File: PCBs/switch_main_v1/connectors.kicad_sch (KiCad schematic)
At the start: 14 parts, among them J1101 76825-0004, J1102 PJ-002AH, J1103 Conn_ST_STDC14, Q1101 DMTH6016LPSQ-13, U1101 TVS2701DRBR, U1102 MPQ5850GJ-AEC1-Z

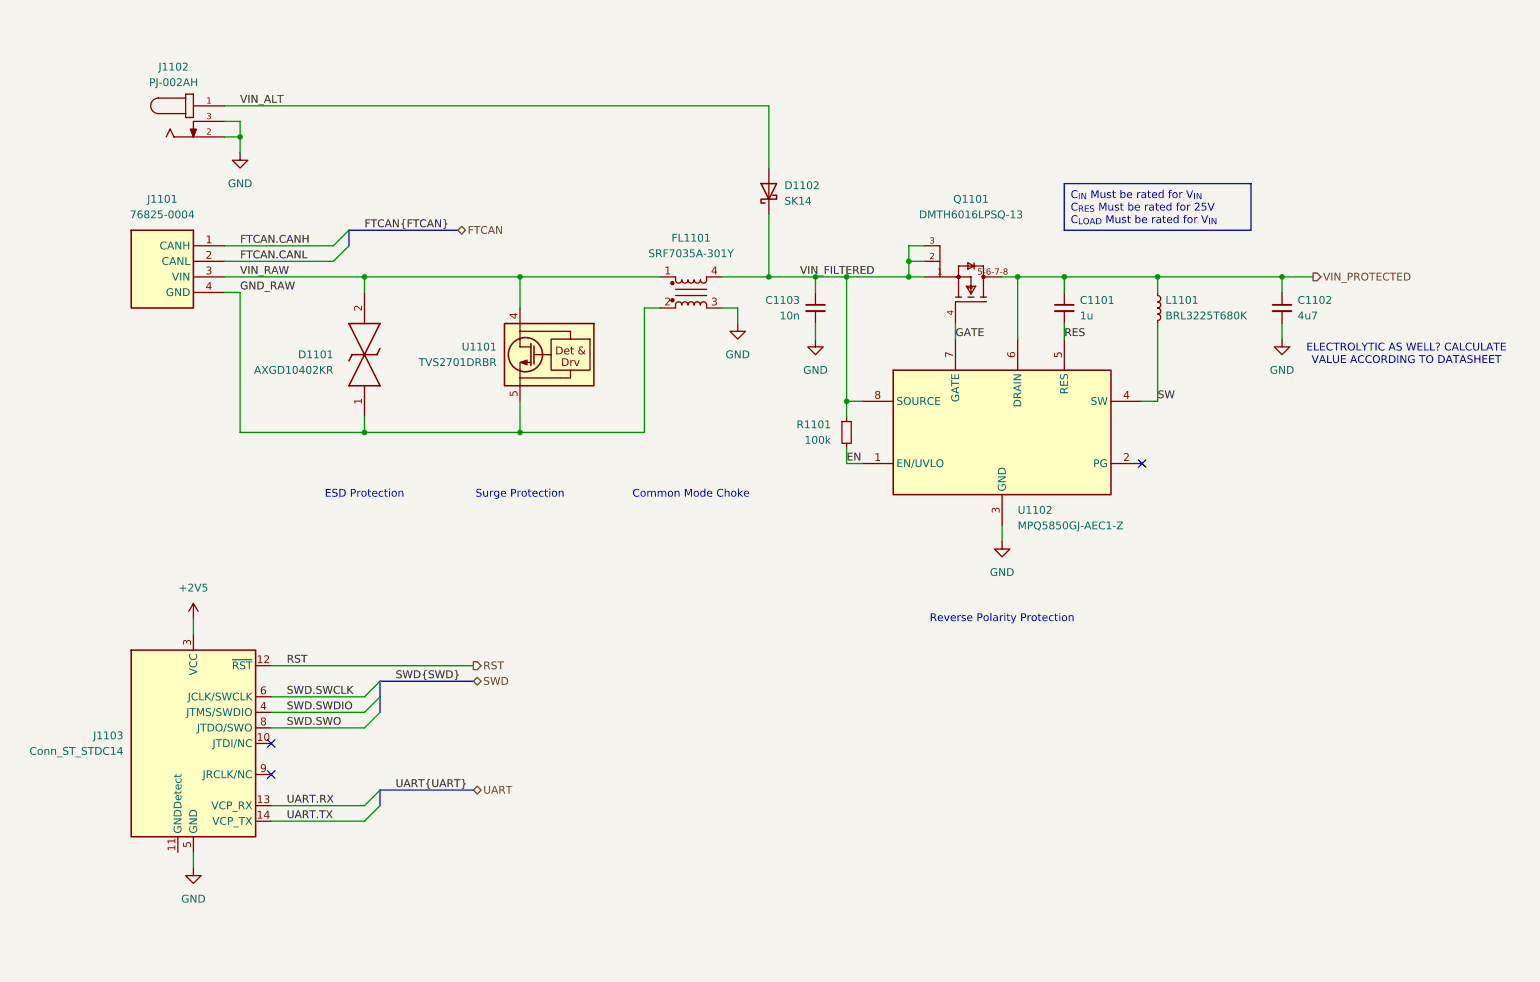
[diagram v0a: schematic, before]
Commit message: Changed MCU to STM32H573IIK3Q
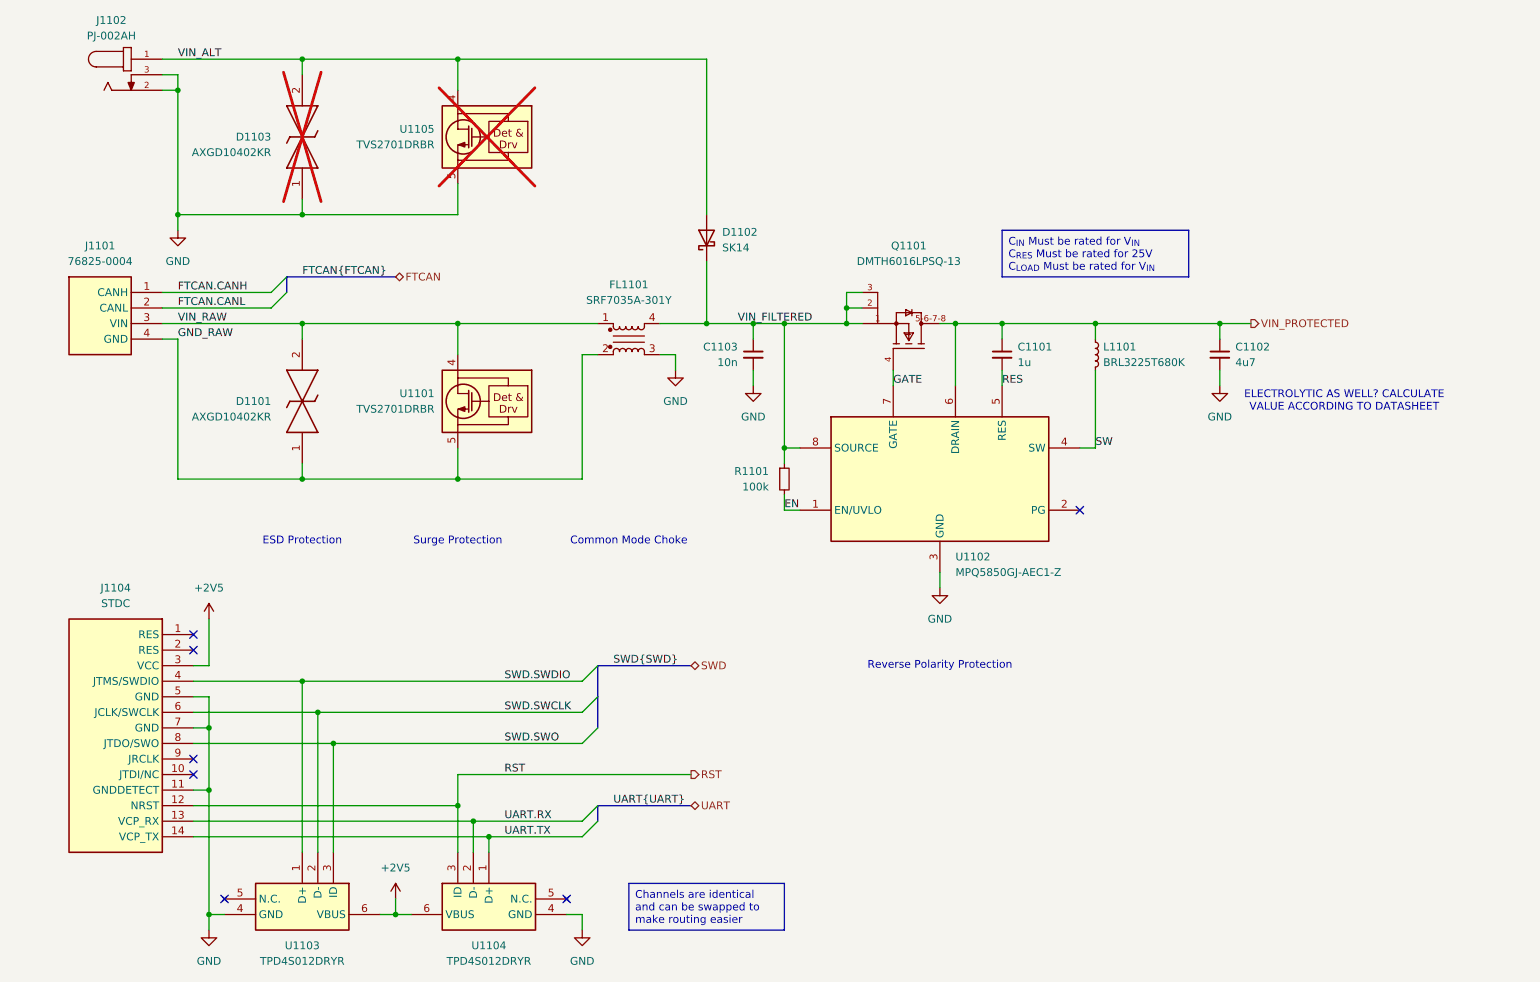
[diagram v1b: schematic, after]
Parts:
- removed J1103: Conn_ST_STDC14, symbol Connector:Conn_ST_STDC14
- added D1103: AXGD10402KR, switch_footprints:DIONM105X51N, symbol AXGD10402KR:AXGD10402KR
- added J1104: STDC, switch_footprints:STDC14, symbol STDC14:STDC14
- added U1103, U1104: TPD4S012DRYR, switch_footprints:TPD4S012DRYR, symbol TPD4S012DRYR:TPD4S012DRYR
- added U1105: TVS2701DRBR, switch_footprints:SON65P300X300X100-9N-D, symbol TVS2701DRBR:TVS2701DRBR
- D1101: footprint DIONM105X51N -> switch_footprints:DIONM105X51N
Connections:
- net +2V5: now also J1104.3 (VCC), U1103.6 (VBUS), U1104.6 (VBUS)
- net GND: now also D1103.1, J1104.11 (GNDDETECT), J1104.5 (GND), J1104.7 (GND), U1103.4 (GND), U1104.4 (GND), U1105.5 (GND), U1105.6 (GND), U1105.7 (GND), U1105.8 (GND)
- net RST: now also J1104.12 (NRST), U1104.3 (ID)
- net SWD.SWCLK: now also J1104.6 (JCLK/SWCLK), U1103.2 (D-)
- net SWD.SWDIO: now also J1104.4 (JTMS/SWDIO), U1103.1 (D+)
- net SWD.SWO: now also J1104.8 (JTDO/SWO), U1103.3 (ID)
- net UART.RX: now also J1104.13 (VCP_RX), U1104.2 (D-)
- net UART.TX: now also J1104.14 (VCP_TX), U1104.1 (D+)
- net VIN_ALT: now also D1103.2, U1105.1 (IN), U1105.2 (IN), U1105.3 (IN), U1105.4 (IN)
- no-connect marks 3 -> 7
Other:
- moved on the sheet: C1101, C1102, C1103, D1101, D1102, FL1101, J1101, J1102, L1101, Q1101, R1101, U1101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
